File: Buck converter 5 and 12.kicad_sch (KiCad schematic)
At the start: 37 parts

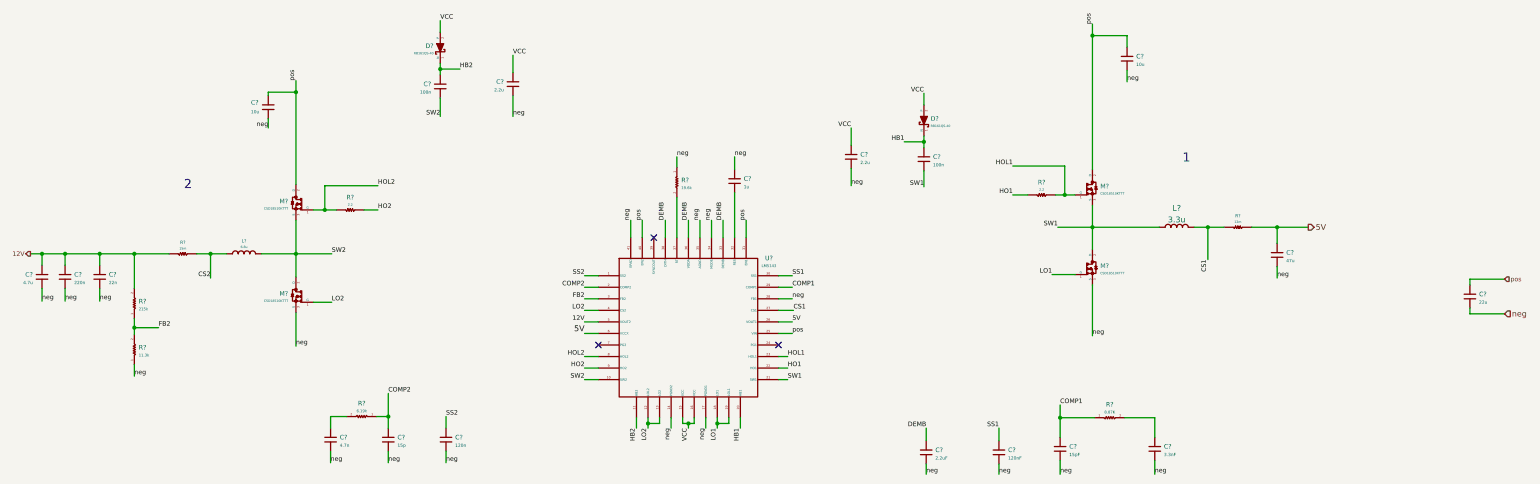
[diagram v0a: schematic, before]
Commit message: reference designator added
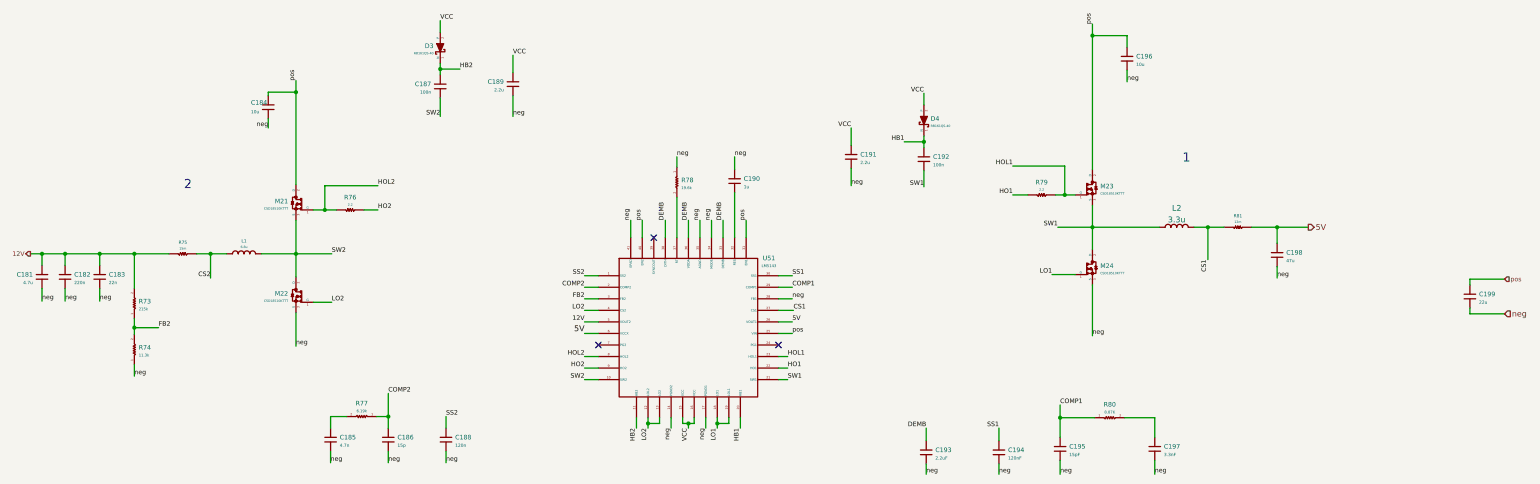
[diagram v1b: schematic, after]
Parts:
- gave numbers to parts that had none: 37

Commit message: changing some capacitors
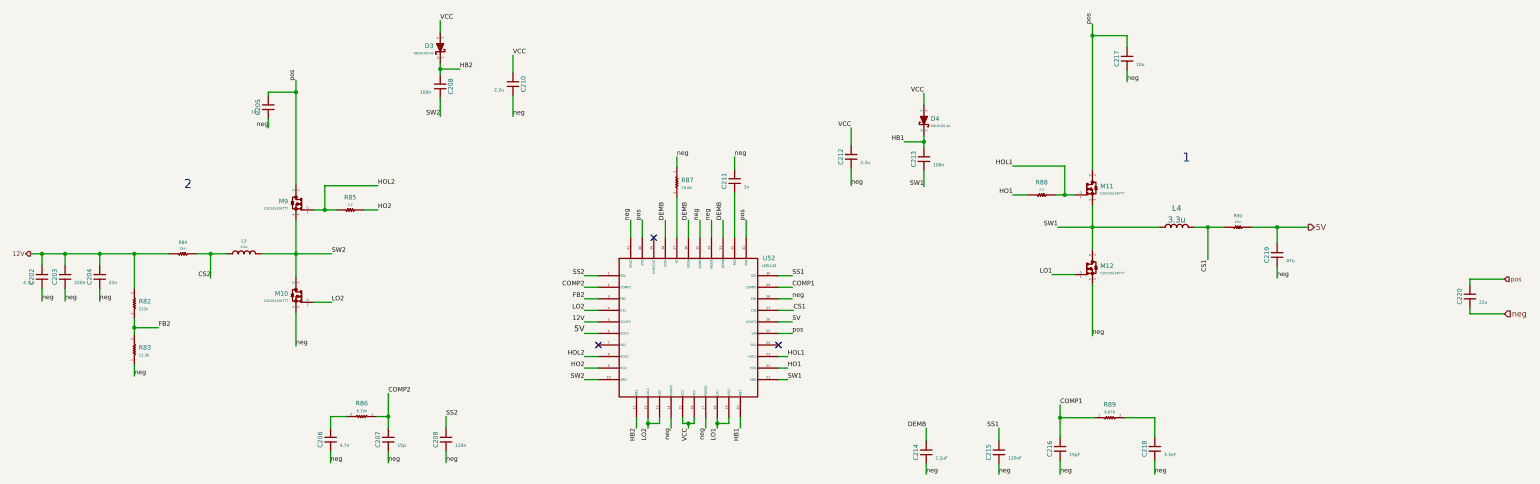
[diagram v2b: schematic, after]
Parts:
- C202: renamed from C181; symbol Capacitors:C0603X105J4RACTU -> Capacitors:C0603xxxxxxxxxxx
- C203: renamed from C182; symbol Capacitors:C0603X105J4RACTU -> Capacitors:C0603xxxxxxxxxxx
- C204: renamed from C183; symbol Capacitors:C0603X105J4RACTU -> Capacitors:C0603xxxxxxxxxxx
- C205: renamed from C184; symbol Capacitors:C0603X105J4RACTU -> Capacitors:C0603xxxxxxxxxxx
- C206: renamed from C185; symbol Capacitors:C0603X105J4RACTU -> Capacitors:C0603xxxxxxxxxxx
- C207: renamed from C186; symbol Capacitors:C0603X105J4RACTU -> Capacitors:C0603xxxxxxxxxxx
- C208: renamed from C187; symbol Capacitors:C0603X105J4RACTU -> Capacitors:C0603xxxxxxxxxxx
- C209: renamed from C188; symbol Capacitors:C0603X105J4RACTU -> Capacitors:C0603xxxxxxxxxxx
- C210: renamed from C189; symbol Capacitors:C0603X105J4RACTU -> Capacitors:C0603xxxxxxxxxxx
- C211: renamed from C190; symbol Capacitors:C0603X105J4RACTU -> Capacitors:C0603xxxxxxxxxxx
- C212: renamed from C191; symbol Capacitors:C0603X105J4RACTU -> Capacitors:C0603xxxxxxxxxxx
- C213: renamed from C192; symbol Capacitors:C0603X105J4RACTU -> Capacitors:C0603xxxxxxxxxxx
- C214: renamed from C193; symbol Capacitors:C0603X105J4RACTU -> Capacitors:C0603xxxxxxxxxxx
- C215: renamed from C194; symbol Capacitors:C0603X105J4RACTU -> Capacitors:C0603xxxxxxxxxxx
- C216: renamed from C195; symbol Capacitors:C0603X105J4RACTU -> Capacitors:C0603xxxxxxxxxxx
- C217: renamed from C196; symbol Capacitors:C0603X105J4RACTU -> Capacitors:C0603xxxxxxxxxxx
- C218: renamed from C197; symbol Capacitors:C0603X105J4RACTU -> Capacitors:C0603xxxxxxxxxxx
- C219: renamed from C198; symbol Capacitors:C0603X105J4RACTU -> Capacitors:C0603xxxxxxxxxxx
- C220: renamed from C199; symbol Capacitors:C0603X105J4RACTU -> Capacitors:C0603xxxxxxxxxxx
- renumbered L1 to L3, L2 to L4, M22 to M10, M23 to M11, M24 to M12, M21 to M9, R73 to R82, R74 to R83, R75 to R84, R76 to R85, R77 to R86, R78 to R87, R79 to R88, R80 to R89, R81 to R90, U51 to U52

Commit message: base schematic and PCB made
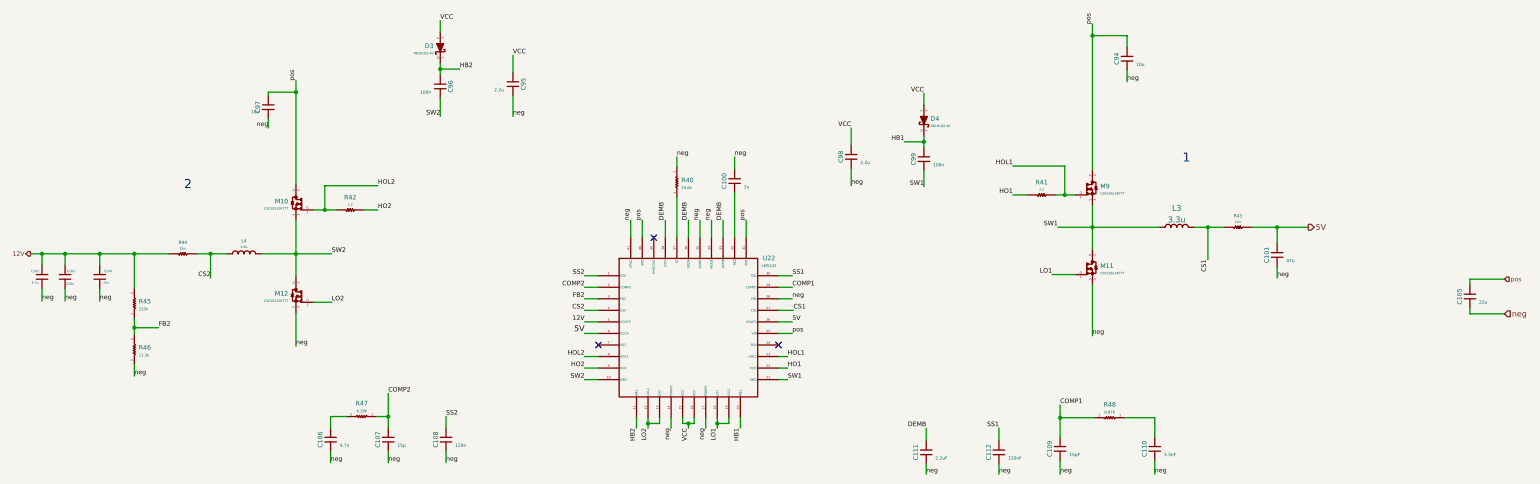
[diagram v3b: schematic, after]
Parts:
- C100: renamed from C211; footprint my_footprints:C0603X105J4RACTU -> Capacitors:C0603X105J4RACTU
- C101: renamed from C219; footprint my_footprints:C0603X105J4RACTU -> Capacitors:C0603X105J4RACTU
- C102: renamed from C202; footprint my_footprints:C0603X105J4RACTU -> Capacitors:C0603X105J4RACTU
- C103: renamed from C203; footprint my_footprints:C0603X105J4RACTU -> Capacitors:C0603X105J4RACTU
- C104: renamed from C204; footprint my_footprints:C0603X105J4RACTU -> Capacitors:C0603X105J4RACTU
- C105: renamed from C220; footprint my_footprints:C0603X105J4RACTU -> Capacitors:C0603X105J4RACTU
- C106: renamed from C206; footprint my_footprints:C0603X105J4RACTU -> Capacitors:C0603X105J4RACTU
- C107: renamed from C207; footprint my_footprints:C0603X105J4RACTU -> Capacitors:C0603X105J4RACTU
- C108: renamed from C209; footprint my_footprints:C0603X105J4RACTU -> Capacitors:C0603X105J4RACTU
- C109: renamed from C216; footprint my_footprints:C0603X105J4RACTU -> Capacitors:C0603X105J4RACTU
- C110: renamed from C218; footprint my_footprints:C0603X105J4RACTU -> Capacitors:C0603X105J4RACTU
- C111: renamed from C214; footprint my_footprints:C0603X105J4RACTU -> Capacitors:C0603X105J4RACTU
- C112: renamed from C215; footprint my_footprints:C0603X105J4RACTU -> Capacitors:C0603X105J4RACTU
- C94: renamed from C217; footprint my_footprints:C0603X105J4RACTU -> Capacitors:C0603X105J4RACTU
- C95: renamed from C210; footprint my_footprints:C0603X105J4RACTU -> Capacitors:C0603X105J4RACTU
- C96: renamed from C208; footprint my_footprints:C0603X105J4RACTU -> Capacitors:C0603X105J4RACTU
- C97: renamed from C205; footprint my_footprints:C0603X105J4RACTU -> Capacitors:C0603X105J4RACTU
- C98: renamed from C212; footprint my_footprints:C0603X105J4RACTU -> Capacitors:C0603X105J4RACTU
- C99: renamed from C213; footprint my_footprints:C0603X105J4RACTU -> Capacitors:C0603X105J4RACTU
- D3, D4: footprint my_footprints:RB161QS-40T18R -> Diodes:RB161QS-40T18R; symbol diodes:RB161QS-40 -> Diodes:RB161QS-40
- L3: renamed from L4; footprint (none) -> Inductors:SBC9-2R2-792
- L4: renamed from L3; footprint (none) -> Inductors:SBC9-2R2-792
- M10: renamed from M9; footprint my_footprints:CSD18510KTTT -> E-MOSFETs:CSD18510KTTT
- M11: renamed from M12; footprint my_footprints:CSD18510KTTT -> E-MOSFETs:CSD18510KTTT
- M12: renamed from M10; footprint my_footprints:CSD18510KTTT -> E-MOSFETs:CSD18510KTTT
- M9: renamed from M11; footprint my_footprints:CSD18510KTTT -> E-MOSFETs:CSD18510KTTT
- R40: renamed from R87; footprint my_footprints:MCR03EZPFX -> Resistors:MCR03EZPFX; symbol resistors:MCR03EZPFX -> Resistors:MCR03EZPFX
- R41: renamed from R88; footprint my_footprints:MCR03EZPFL -> Resistors:MCR03EZPFL; symbol resistors:MCR03EZPFL -> Resistors:MCR03EZPFL
- R42: renamed from R85; footprint my_footprints:MCR03EZPFL -> Resistors:MCR03EZPFL; symbol resistors:MCR03EZPFL -> Resistors:MCR03EZPFL
- R43: renamed from R90; footprint my_footprints:UCR18EVH -> Resistors:UCR18EVH; symbol resistors:UCR18EVH -> Resistors:UCR18EVH
- R44: renamed from R84; footprint my_footprints:UCR18EVH -> Resistors:UCR18EVH; symbol resistors:UCR18EVH -> Resistors:UCR18EVH
- R45: renamed from R82; footprint my_footprints:MCR03EZPFX -> Resistors:MCR03EZPFX; symbol resistors:MCR03EZPFX -> Resistors:MCR03EZPFX
- R46: renamed from R83; footprint my_footprints:MCR03EZPFX -> Resistors:MCR03EZPFX; symbol resistors:MCR03EZPFX -> Resistors:MCR03EZPFX
- R47: renamed from R86; footprint my_footprints:MCR03EZPFX -> Resistors:MCR03EZPFX; symbol resistors:MCR03EZPFX -> Resistors:MCR03EZPFX
- R48: renamed from R89; footprint my_footprints:MCR03EZPFX -> Resistors:MCR03EZPFX; symbol resistors:MCR03EZPFX -> Resistors:MCR03EZPFX
- U22: renamed from U52; footprint my_footprints:LM5143RHAR -> ICs:LM5143RHAR
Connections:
- net CS2: now also U22.4 (CS2)
- net LO2: no longer U22.4 (CS2)

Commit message: minor changes
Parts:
- C100: value 1u -> (none); footprint Capacitors:C0603X105J4RACTU -> (none)
- C101: value 47u -> (none); footprint Capacitors:C0603X105J4RACTU -> (none)
- C102: value 4.7u -> (none); footprint Capacitors:C0603X105J4RACTU -> (none)
- C103: value 220n -> (none); footprint Capacitors:C0603X105J4RACTU -> (none)
- C104: value 22n -> (none); footprint Capacitors:C0603X105J4RACTU -> (none)
- C105: value 22u -> (none); footprint Capacitors:C0603X105J4RACTU -> (none)
- C106: value 4.7n -> (none); footprint Capacitors:C0603X105J4RACTU -> (none)
- C107: value 15p -> (none); footprint Capacitors:C0603X105J4RACTU -> (none)
- C108: value 120n -> (none); footprint Capacitors:C0603X105J4RACTU -> (none)
- C109: value 15pF -> (none); footprint Capacitors:C0603X105J4RACTU -> (none)
- C110: value 3.3nF -> (none); footprint Capacitors:C0603X105J4RACTU -> (none)
- C111: value 2.2uF -> (none); footprint Capacitors:C0603X105J4RACTU -> (none)
- C112: value 120nF -> (none); footprint Capacitors:C0603X105J4RACTU -> (none)
- C94, C97: value 10u -> (none); footprint Capacitors:C0603X105J4RACTU -> (none)
- C95, C98: value 2.2u -> (none); footprint Capacitors:C0603X105J4RACTU -> (none)
- C96, C99: value 100n -> (none); footprint Capacitors:C0603X105J4RACTU -> (none)
- D3, D4: value RB161QS-40 -> (none); footprint Diodes:RB161QS-40T18R -> (none)
- L3: value 3.3u -> (none); footprint Inductors:SBC9-2R2-792 -> (none)
- L4: value 6.8u -> (none); footprint Inductors:SBC9-2R2-792 -> (none)
- M10, M11, M12, M9: value CSD18510KTTT -> (none); footprint E-MOSFETs:CSD18510KTTT -> (none)
- R40: value 19.6k -> (none); footprint Resistors:MCR03EZPFX -> (none)
- R41, R42: value 2.2 -> (none); footprint Resistors:MCR03EZPFL -> (none)
- R43: value 12m -> (none); footprint Resistors:UCR18EVH -> (none)
- R44: value 15m -> (none); footprint Resistors:UCR18EVH -> (none)
- R45: value 215k -> (none); footprint Resistors:MCR03EZPFX -> (none)
- R46: value 11.3k -> (none); footprint Resistors:MCR03EZPFX -> (none)
- R47: value 6.19k -> (none); footprint Resistors:MCR03EZPFX -> (none)
- R48: value 8.87K -> (none); footprint Resistors:MCR03EZPFX -> (none)
- U22: value LM5143 -> (none); footprint ICs:LM5143RHAR -> (none)
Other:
- company: (none) -> 3D ROBOT
- title: 3D robot project - electronics -> Base circuit - TH

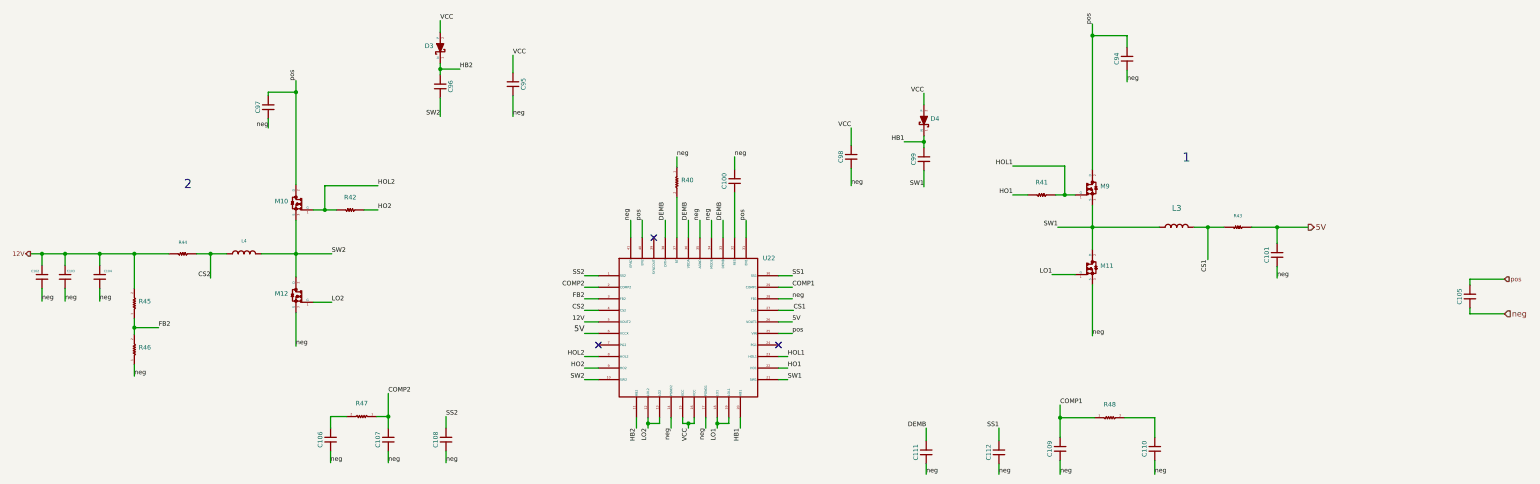
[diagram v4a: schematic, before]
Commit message: make a TH version of the base PCB for testing purposes...
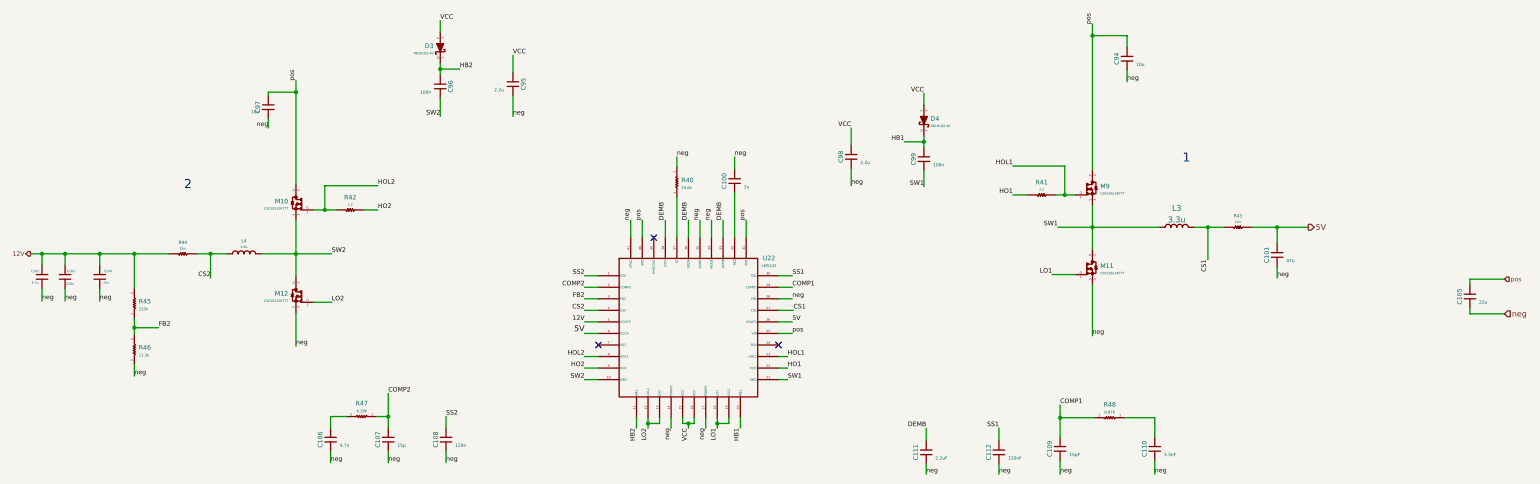
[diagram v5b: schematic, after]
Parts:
- C100: value (none) -> 1u; footprint (none) -> Capacitors:C0603X105J4RACTU
- C101: value (none) -> 47u; footprint (none) -> Capacitors:C0603X105J4RACTU
- C102: value (none) -> 4.7u; footprint (none) -> Capacitors:C0603X105J4RACTU
- C103: value (none) -> 220n; footprint (none) -> Capacitors:C0603X105J4RACTU
- C104: value (none) -> 22n; footprint (none) -> Capacitors:C0603X105J4RACTU
- C105: value (none) -> 22u; footprint (none) -> Capacitors:C0603X105J4RACTU
- C106: value (none) -> 4.7n; footprint (none) -> Capacitors:C0603X105J4RACTU
- C107: value (none) -> 15p; footprint (none) -> Capacitors:C0603X105J4RACTU
- C108: value (none) -> 120n; footprint (none) -> Capacitors:C0603X105J4RACTU
- C109: value (none) -> 15pF; footprint (none) -> Capacitors:C0603X105J4RACTU
- C110: value (none) -> 3.3nF; footprint (none) -> Capacitors:C0603X105J4RACTU
- C111: value (none) -> 2.2uF; footprint (none) -> Capacitors:C0603X105J4RACTU
- C112: value (none) -> 120nF; footprint (none) -> Capacitors:C0603X105J4RACTU
- C94, C97: value (none) -> 10u; footprint (none) -> Capacitors:C0603X105J4RACTU
- C95, C98: value (none) -> 2.2u; footprint (none) -> Capacitors:C0603X105J4RACTU
- C96, C99: value (none) -> 100n; footprint (none) -> Capacitors:C0603X105J4RACTU
- D3, D4: value (none) -> RB161QS-40; footprint (none) -> Diodes:RB161QS-40T18R
- L3: value (none) -> 3.3u; footprint (none) -> Inductors:SBC9-2R2-792
- L4: value (none) -> 6.8u; footprint (none) -> Inductors:SBC9-2R2-792
- M10, M11, M12, M9: value (none) -> CSD18510KTTT; footprint (none) -> E-MOSFETs:CSD18510KTTT
- R40: value (none) -> 19.6k; footprint (none) -> Resistors:MCR03EZPFX
- R41, R42: value (none) -> 2.2; footprint (none) -> Resistors:MCR03EZPFL
- R43: value (none) -> 12m; footprint (none) -> Resistors:UCR18EVH
- R44: value (none) -> 15m; footprint (none) -> Resistors:UCR18EVH
- R45: value (none) -> 215k; footprint (none) -> Resistors:MCR03EZPFX
- R46: value (none) -> 11.3k; footprint (none) -> Resistors:MCR03EZPFX
- R47: value (none) -> 6.19k; footprint (none) -> Resistors:MCR03EZPFX
- R48: value (none) -> 8.87K; footprint (none) -> Resistors:MCR03EZPFX
- U22: value (none) -> LM5143; footprint (none) -> ICs:LM5143RHAR
